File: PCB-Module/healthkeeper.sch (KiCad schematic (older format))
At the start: 28 parts, among them J1 RPI Conn, J2 24VDC-IN, J3 CTRL VALVE, J4 BAT Sense, J5 7\"LCD Screen, J6 Flow Conn, J7 DpFlow Selector, Q1 IRF540NLPBF, U1 MCP4921-EP, U2 MCP6241, U3 TEN20-2411WIN, U4 MCP3208, U5 HSCSAAN001PDAA5, U6 HSCSAAN001PDAA5, U7 SDP816-125Pa

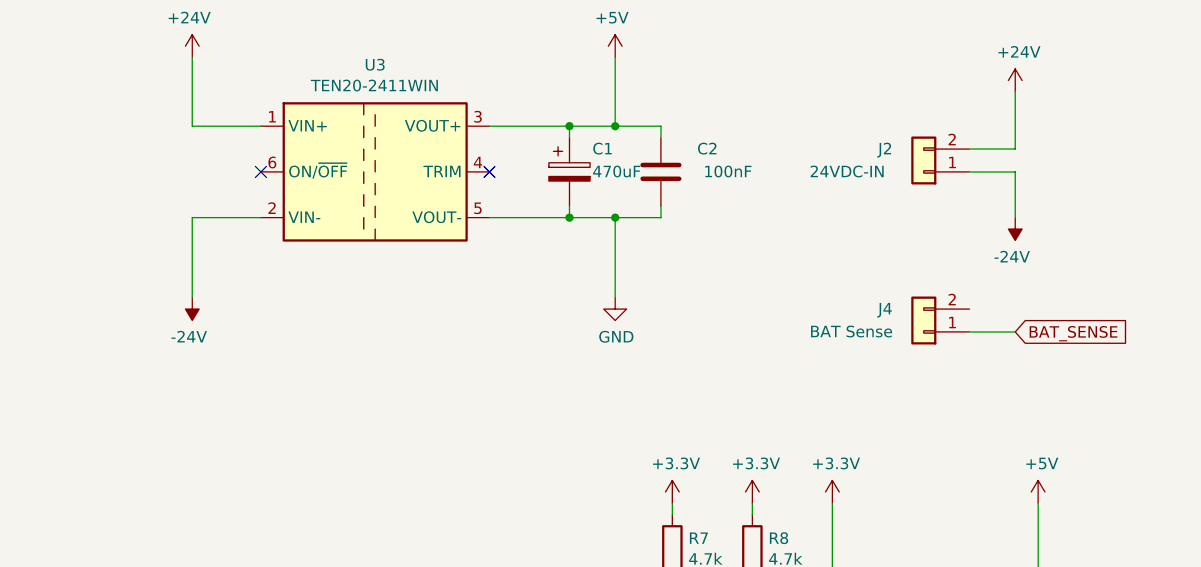
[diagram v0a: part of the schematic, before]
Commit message: Joint 24V and 5V ground
Error in the Rev 1.3 design as the 24V and 5V power weren't connected. This leads to an issue with the valve control.
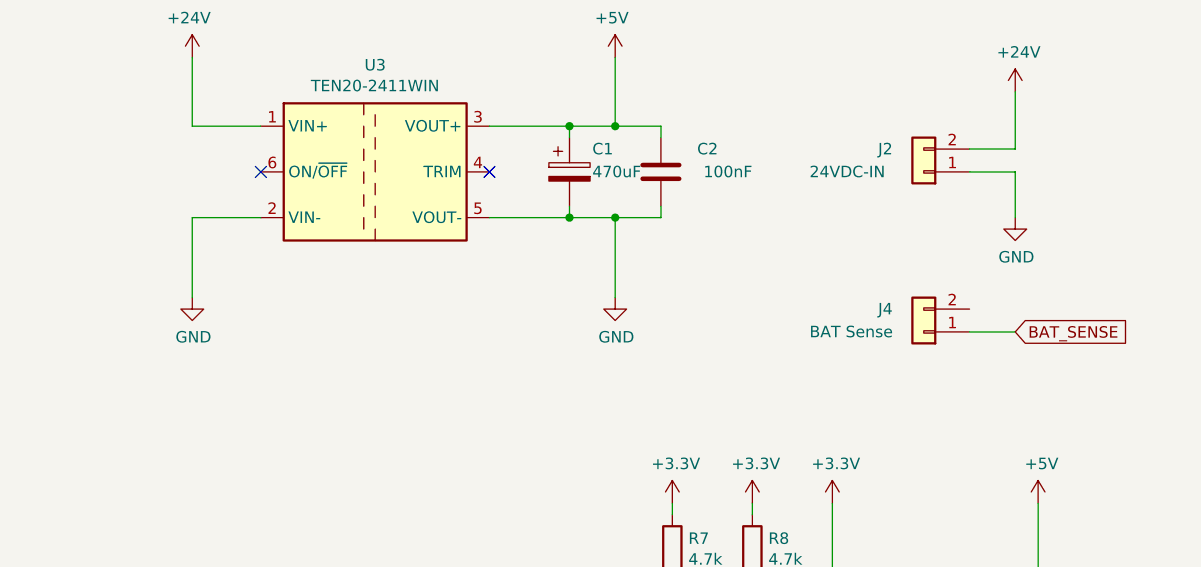
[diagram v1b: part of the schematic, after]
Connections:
- net -24V is gone; now on net GND: J2.1 (Pin_1), U3.2 (VIN-)
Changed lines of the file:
@@
 Wire Wire Line
 	7900 2300 7600 2300
-Wire Wire Line
-	7600 2300 7600 2650
 $Comp
 L power:GND #PWR0116
@@
 	9650 2300 9450 2300
 Connection ~ 9450 2300
-$Comp
-L power:-24V #PWR0110
-U 1 1 5F9834C7
-P 7600 2650
-F 0 "#PWR0110" H 7600 2750 50  0001 C CNN
-F 1 "-24V" H 7615 2823 50  0000 C CNN
-F 2 "" H 7600 2650 50  0001 C CNN
-F 3 "" H 7600 2650 50  0001 C CNN
-	1    7600 2650
-	-1   0    0    1
-$EndComp
-$Comp
-L power:-24V #PWR0115
-U 1 1 5F98406A
-P 11200 2300
-F 0 "#PWR0115" H 11200 2400 50  0001 C CNN
-F 1 "-24V" H 11215 2473 50  0000 C CNN
-F 2 "" H 11200 2300 50  0001 C CNN
-F 3 "" H 11200 2300 50  0001 C CNN
-	1    11200 2300
-	-1   0    0    1
-$EndComp
 Wire Wire Line
 	3950 6450 2750 6450
@@
 Wire Wire Line
 	3650 6150 3950 6150
+$Comp
+L power:GND #PWR?
+U 1 1 5FCB018A
+P 7600 2650
+F 0 "#PWR?" H 7600 2400 50  0001 C CNN
+F 1 "GND" H 7605 2477 50  0000 C CNN
+F 2 "" H 7600 2650 50  0001 C CNN
+F 3 "" H 7600 2650 50  0001 C CNN
+	1    7600 2650
+	1    0    0    -1
+$EndComp
+Wire Wire Line
+	7600 2300 7600 2650
+$Comp
+L power:GND #PWR?
+U 1 1 5FCEDB4F
+P 11200 2300
+F 0 "#PWR?" H 11200 2050 50  0001 C CNN
+F 1 "GND" H 11205 2127 50  0000 C CNN
+F 2 "" H 11200 2300 50  0001 C CNN
+F 3 "" H 11200 2300 50  0001 C CNN
+	1    11200 2300
+	1    0    0    -1
+$EndComp
 $EndSCHEMATC

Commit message: Added RaspberryPI to the Footprint library
Added RaspberryPI to the Footprint library
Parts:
- J1: footprint Module:Raspberry_Pi4 -> Raspberry_Pi4:Raspberry_Pi4
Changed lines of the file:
@@
 F 0 "J1" H 10800 6200 50  0000 C CNN
 F 1 "RPI Conn" H 10900 6100 50  0000 C CNN
-F 2 "Module:Raspberry_Pi4" H 10800 5050 50  0001 C CNN
+F 2 "Raspberry_Pi4:Raspberry_Pi4" H 10800 5050 50  0001 C CNN
 F 3 "~" H 10800 5050 50  0001 C CNN
 	1    10800 5050
